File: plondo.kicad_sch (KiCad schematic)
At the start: 17 parts, among them J1 AVR-ISP-6, J2 USB C Port, U1 ATmega32A-P, X1 XTAL

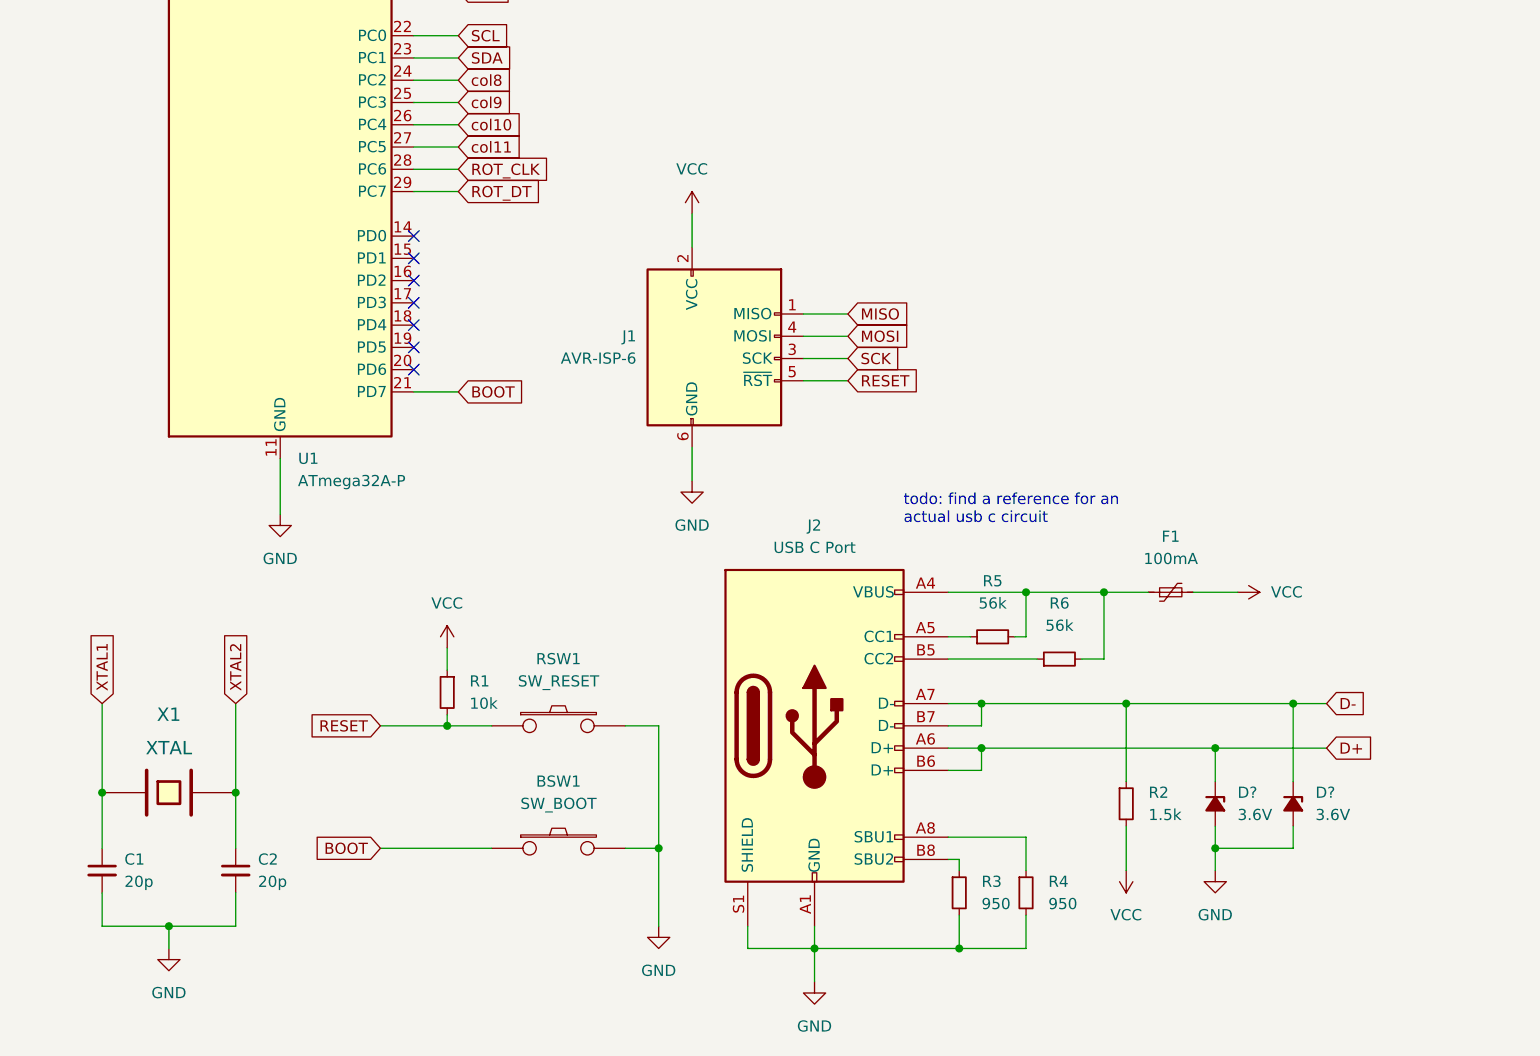
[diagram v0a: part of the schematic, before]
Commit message: add libs as submodules, fix up usb c wiring
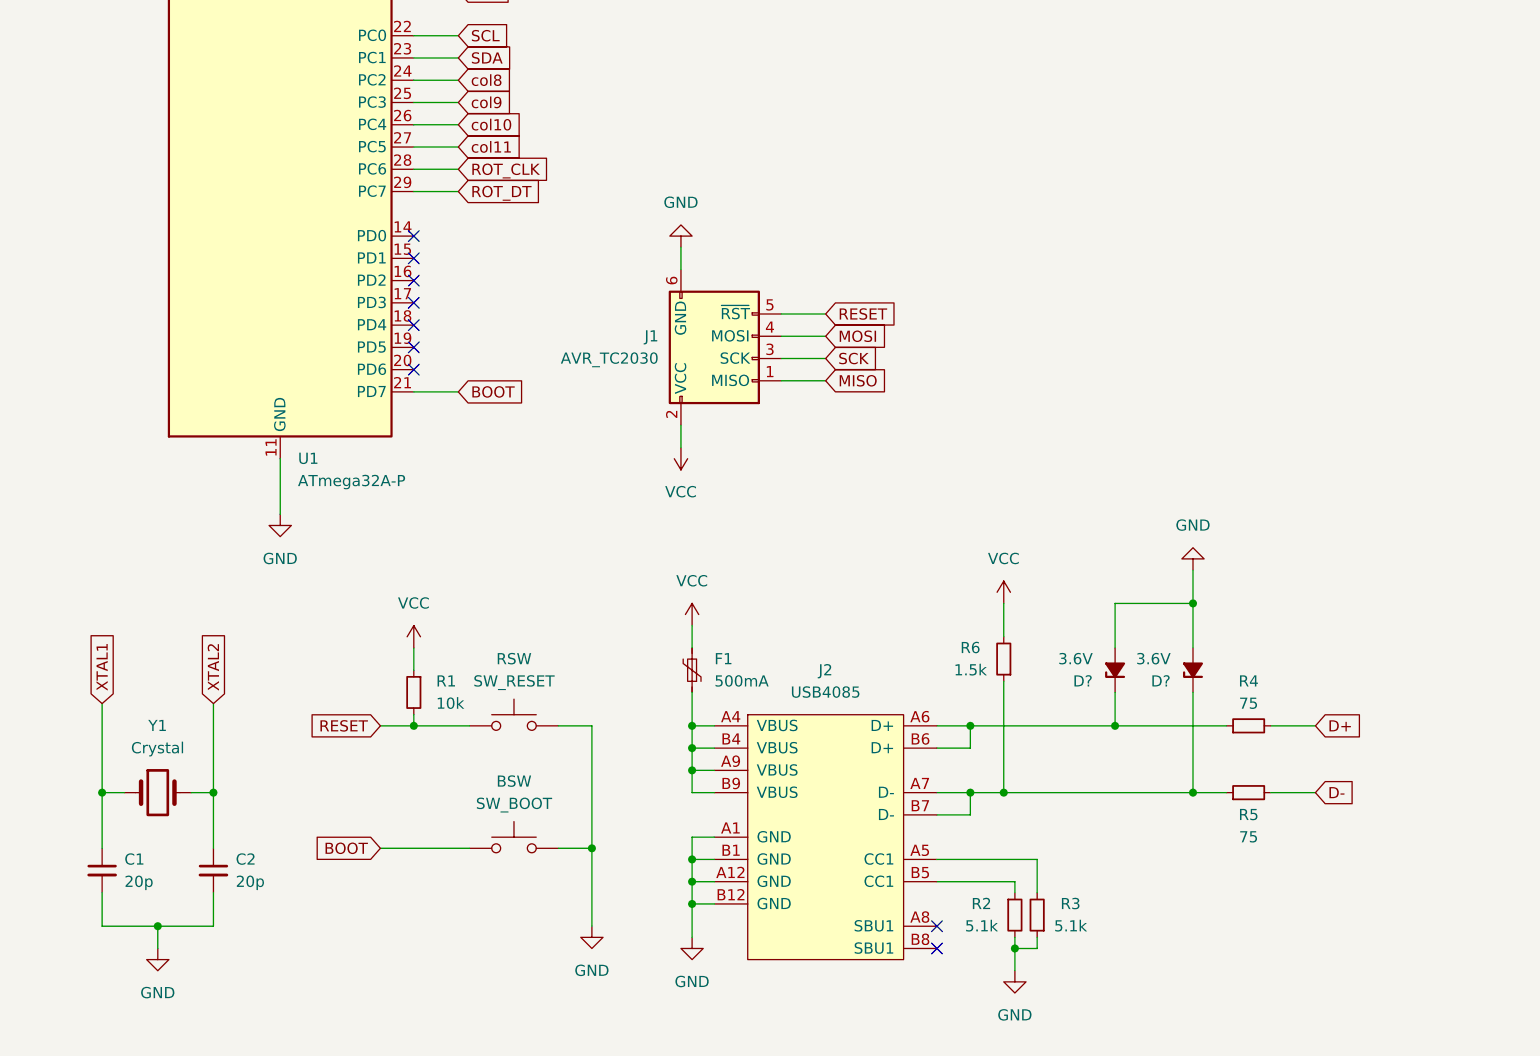
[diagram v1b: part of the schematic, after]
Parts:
- removed BSW1: SW_BOOT, symbol keyboard_parts:SW_PUSH
- removed J1: AVR-ISP-6, symbol Connector:AVR-ISP-6
- removed J2: USB C Port, symbol Connector:USB_C_Receptacle_USB2.0
- removed RSW1: SW_RESET, symbol keyboard_parts:SW_PUSH
- removed X1: XTAL, symbol keyboard_parts:XTAL
- added BSW: SW_BOOT, symbol Switch:SW_Push
- added J1: AVR_TC2030, marbastlib-various:CON_TC2030_outlined, symbol marbastlib-various:AVR_TC2030
- added J2: USB4085, agg:USB4085, symbol agg-kicad:USB4085
- added RSW: SW_RESET, symbol Switch:SW_Push
- added Y1: Crystal, symbol Device:Crystal
- F1: value 100mA -> 500mA
- R2: value 1.5k -> 5.1k
- R3: value 950 -> 5.1k
- R4: value 950 -> 75
- R5: value 56k -> 75
- R6: value 56k -> 1.5k
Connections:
- net BOOT: now also BSW.1
- net D+: now also R4.2; no longer D?.1 (K)
- net D-: now also R5.2; no longer D?.1 (K), R2.1
- net GND: now also R2.2, R3.1, BSW.2, J1.6 (GND), J2.A1 (GND), J2.A12 (GND), J2.B1 (GND), J2.B12 (GND), RSW.2; no longer R3.2, R4.2
- net MISO: now also J1.1 (MISO)
- net MOSI: now also J1.4 (MOSI)
- net RESET: now also J1.5 (~{RST}), RSW.1
- net SCK: now also J1.3 (SCK)
- net VCC: now also R6.2, J1.2 (VCC); no longer R2.2
- net XTAL1: now also Y1.1
- net XTAL2: now also Y1.2
- net at R4.1: now also D?.1 (K), J2.A6 (D+), J2.B6 (D+)
- net at R6.1: now also D?.1 (K), R5.1, J2.A7 (D-), J2.B7 (D-)
- new net: J2.B5 (CC1), R2.1
- new net: F1.1, J2.A4 (VBUS), J2.A9 (VBUS), J2.B4 (VBUS), J2.B9 (VBUS)
- new net: J2.A5 (CC1), R3.2
- no-connect marks 8 -> 10
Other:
- note removed: "todo: find a reference for an actual usb c circuit"
- moved on the sheet: C2, D?, F1, R1

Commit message: complete main circuitry
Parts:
- added C3: 4.7u, symbol Device:C_Polarized_Small
- added C4, C5: 0.1u, symbol Device:C_Small
- added LED1: PWR_LED, symbol agg-kicad:LED
- added R7: 1.5k, symbol Device:R_Small
- gave numbers to parts that had none: 2
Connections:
- net GND: now also C3.2, C4.2, C5.2, R7.1
- net VCC: now also C3.1, C4.1, C5.1, LED1.2
- new net: LED1.1, R7.2

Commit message: add indicator LEDs
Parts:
- added LED2: IND_LED1, symbol agg-kicad:LED
- added LED3: IND_LED2, symbol agg-kicad:LED
- added LED4: IND_LED3, symbol agg-kicad:LED
- added R10, R8, R9: 1.5k, symbol Device:R_Small
- renumbered BSW to BSW1, RSW to RSW1
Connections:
- net GND: now also R10.1, R8.1, R9.1
- net IND1: now reaches U1.14 (PD0)
- net IND1: now also LED2.2
- net IND2: now reaches U1.15 (PD1)
- net IND2: now also LED3.2
- net IND3: now reaches U1.16 (PD2)
- net IND3: now also LED4.2
- net col0 renamed COL0
- net col1 renamed COL1
- net col10 renamed COL10
- net col11 renamed COL11
- net col2 renamed COL2
- net col3 renamed COL3
- net col4 renamed COL4
- net col5 renamed COL5
- net col6 renamed COL6
- net col7 renamed COL7
- net col8 renamed COL8
- net col9 renamed COL9
- net row0 renamed ROW0
- net row1 renamed ROW1
- net row2 renamed ROW2
- net row3 renamed ROW3
- net row4 renamed ROW4
- new net: LED2.1, R8.2
- new net: LED4.1, R10.2
- new net: LED3.1, R9.2
- no-connect marks 10 -> 7
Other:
- moved on the sheet: LED1, R7

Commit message: add missing connections + oled
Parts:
- added OL1: OLED, kbd:OLED_1side, symbol kbd:OLED
- BSW1, RSW1: footprint (none) -> Button_Switch_THT:SW_PUSH_6mm_H4.3mm
- C1, C2, C3, C4, C5, D48, D49: footprint (none) -> Diode_THT:D_DO-35_SOD27_P7.62mm_Horizontal
- F1: footprint (none) -> Fuse:Fuse_BelFuse_0ZRE0100FF_L18.7mm_W5.1mm
- LED1, LED2, LED3, LED4: footprint (none) -> LED_THT:LED_D3.0mm
- R1, R10, R2, R3, R4, R5, R6, R7, R8, R9: footprint (none) -> Resistor_THT:R_Axial_DIN0207_L6.3mm_D2.5mm_P7.62mm_Horizontal
- U1: footprint Package_DIP:DIP-40_W15.24mm -> Package_DIP:DIP-40_W15.24mm_Socket
- Y1: footprint (none) -> Crystal:Resonator-2Pin_W10.0mm_H5.0mm
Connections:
- net D+: now also U1.19 (PD5)
- net D-: now also U1.20 (PD6)
- net GND: now also OL1.4 (GND)
- net SCL: now also OL1.2 (SCL)
- net SDA: now also OL1.1 (SDA)
- net VCC: now also OL1.3 (VCC)
- no-connect marks 7 -> 5

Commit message: first pass of pcb layout, fix footprints
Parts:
- C1, C2: footprint Diode_THT:D_DO-35_SOD27_P7.62mm_Horizontal -> Capacitor_THT:C_Disc_D7.5mm_W4.4mm_P5.00mm
- C3: footprint Diode_THT:D_DO-35_SOD27_P7.62mm_Horizontal -> Capacitor_THT:CP_Radial_D4.0mm_P1.50mm
- C4, C5: footprint Diode_THT:D_DO-35_SOD27_P7.62mm_Horizontal -> Capacitor_THT:C_Disc_D5.0mm_W2.5mm_P5.00mm
- F1: footprint Fuse:Fuse_BelFuse_0ZRE0100FF_L18.7mm_W5.1mm -> Fuse:Fuse_Littelfuse_395Series
- J1: footprint marbastlib-various:CON_TC2030_outlined -> Connector_PinHeader_1.27mm:PinHeader_2x03_P1.27mm_Vertical
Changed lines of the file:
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@@
       (effects (font (size 1.27 1.27)) (justify left))
     )
-    (property "Footprint" "Diode_THT:D_DO-35_SOD27_P7.62mm_Horizontal" (id 2) (at 144.78 118.11 0)
+    (property "Footprint" "Capacitor_THT:C_Disc_D5.0mm_W2.5mm_P5.00mm" (id 2) (at 144.78 118.11 0)
       (effects (font (size 1.27 1.27)) hide)
     )
@@
       (effects (font (size 1.27 1.27)) (justify left))
     )
-    (property "Footprint" "Diode_THT:D_DO-35_SOD27_P7.62mm_Horizontal" (id 2) (at 41.91 177.8 0)
+    (property "Footprint" "Capacitor_THT:C_Disc_D7.5mm_W4.4mm_P5.00mm" (id 2) (at 41.91 177.8 0)
       (effects (font (size 1.27 1.27)) hide)
     )
@@
       (effects (font (size 1.27 1.27)) (justify left))
     )
-    (property "Footprint" "Diode_THT:D_DO-35_SOD27_P7.62mm_Horizontal" (id 2) (at 135.89 118.11 0)
+    (property "Footprint" "Capacitor_THT:CP_Radial_D4.0mm_P1.50mm" (id 2) (at 135.89 118.11 0)
       (effects (font (size 1.27 1.27)) hide)
     )
@@
       (effects (font (size 1.27 1.27)) (justify right))
     )
-    (property "Footprint" "Fuse:Fuse_BelFuse_0ZRE0100FF_L18.7mm_W5.1mm" (id 2) (at 95.25 149.86 0)
+    (property "Footprint" "Fuse:Fuse_Littelfuse_395Series" (id 2) (at 95.25 149.86 0)
       (effects (font (size 1.27 1.27)) (justify left) hide)
     )
@@
       (effects (font (size 1.27 1.27)) (justify left))
     )
-    (property "Footprint" "Diode_THT:D_DO-35_SOD27_P7.62mm_Horizontal" (id 2) (at 29.21 177.8 0)
+    (property "Footprint" "Capacitor_THT:C_Disc_D7.5mm_W4.4mm_P5.00mm" (id 2) (at 29.21 177.8 0)
       (effects (font (size 1.27 1.27)) hide)
     )
@@
       (effects (font (size 1.27 1.27)) (justify left))
     )
-    (property "Footprint" "Diode_THT:D_DO-35_SOD27_P7.62mm_Horizontal" (id 2) (at 153.67 118.11 0)
+    (property "Footprint" "Capacitor_THT:C_Disc_D5.0mm_W2.5mm_P5.00mm" (id 2) (at 153.67 118.11 0)
       (effects (font (size 1.27 1.27)) hide)
     )
@@
       (effects (font (size 1.27 1.27)) (justify left))
     )
-    (property "Footprint" "marbastlib-various:CON_TC2030_outlined" (id 2) (at 90.17 118.11 90)
+    (property "Footprint" "Connector_PinHeader_1.27mm:PinHeader_2x03_P1.27mm_Vertical" (id 2) (at 90.17 118.11 90)
       (effects (font (size 1.27 1.27)) hide)
     )
@@
     )
     (path "/4def4295-a27d-4f6d-91bd-6111a548b6a3"
-      (reference "C1") (unit 1) (value "20p") (footprint "Diode_THT:D_DO-35_SOD27_P7.62mm_Horizontal")
+      (reference "C1") (unit 1) (value "20p") (footprint "Capacitor_THT:C_Disc_D7.5mm_W4.4mm_P5.00mm")
     )
     (path "/311a51ef-1d28-43bc-81ee-cf4ad1843df8"
-      (reference "C2") (unit 1) (value "20p") (footprint "Diode_THT:D_DO-35_SOD27_P7.62mm_Horizontal")
+      (reference "C2") (unit 1) (value "20p") (footprint "Capacitor_THT:C_Disc_D7.5mm_W4.4mm_P5.00mm")
     )
     (path "/47b54b0f-a49d-4a9f-a97d-948d6af52935"
-      (reference "C3") (unit 1) (value "4.7u") (footprint "Diode_THT:D_DO-35_SOD27_P7.62mm_Horizontal")
+      (reference "C3") (unit 1) (value "4.7u") (footprint "Capacitor_THT:CP_Radial_D4.0mm_P1.50mm")
     )
     (path "/175f116a-4fab-477c-a9b3-e63c21a71a0a"
-      (reference "C4") (unit 1) (value "0.1u") (footprint "Diode_THT:D_DO-35_SOD27_P7.62mm_Horizontal")
+      (reference "C4") (unit 1) (value "0.1u") (footprint "Capacitor_THT:C_Disc_D5.0mm_W2.5mm_P5.00mm")
     )
     (path "/5bd4309a-7bca-4bc0-bb56-09922d20fbfa"
-      (reference "C5") (unit 1) (value "0.1u") (footprint "Diode_THT:D_DO-35_SOD27_P7.62mm_Horizontal")
+      (reference "C5") (unit 1) (value "0.1u") (footprint "Capacitor_THT:C_Disc_D5.0mm_W2.5mm_P5.00mm")
     )
     (path "/1db02ae6-bdcf-4a52-9b2f-2c1ad11c5a9a/42303839-8286-4f56-9d6b-353218c46182"
@@
     )
     (path "/4a2d7a4d-63d2-4e49-ba54-139faaa3fb67"
-      (reference "F1") (unit 1) (value "500mA") (footprint "Fuse:Fuse_BelFuse_0ZRE0100FF_L18.7mm_W5.1mm")
+      (reference "F1") (unit 1) (value "500mA") (footprint "Fuse:Fuse_Littelfuse_395Series")
     )
     (path "/f0399126-c923-4b6d-8abf-e898f07c35f0"
-      (reference "J1") (unit 1) (value "AVR_TC2030") (footprint "marbastlib-various:CON_TC2030_outlined")
+      (reference "J1") (unit 1) (value "AVR_TC2030") (footprint "Connector_PinHeader_1.27mm:PinHeader_2x03_P1.27mm_Vertical")
     )
     (path "/51ebb439-c6af-468c-965f-964066615b44"

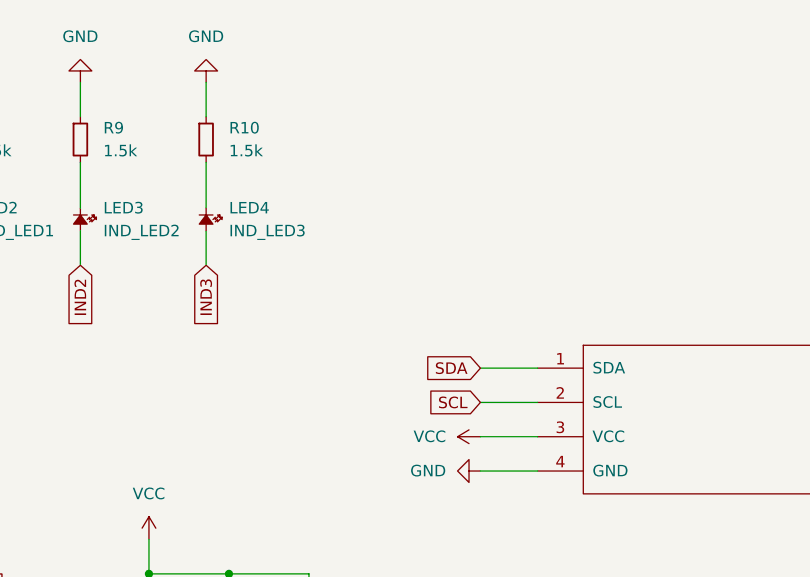
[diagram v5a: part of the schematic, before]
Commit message: add pullups for i2c lines
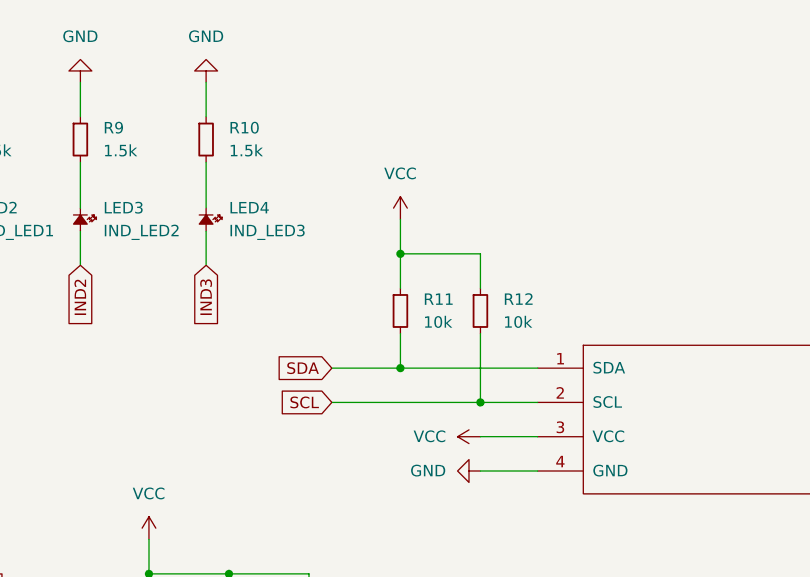
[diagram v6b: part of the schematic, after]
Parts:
- added R11, R12: 10k, Resistor_THT:R_Axial_DIN0207_L6.3mm_D2.5mm_P7.62mm_Horizontal, symbol Device:R_Small
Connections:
- net SCL: now also R12.2
- net SDA: now also R11.2
- net VCC: now also R11.1, R12.1
